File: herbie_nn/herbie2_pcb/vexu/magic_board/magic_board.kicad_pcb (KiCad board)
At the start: 2 copper layers, 70 x 50 mm, 88 parts, among them J1 4P4C, J2 Conn_ARM_JTAG_SWD_10, J3 USB_C_Receptacle_USB2.0_14P, J4 Conn_01x04_Socket, J5 Conn_01x05_Pin, J6 Conn_01x05_Pin, J7 Conn_01x05_Pin, Q2 MMBT3904, U11 74LVC125, U12 AMS1117-5.0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

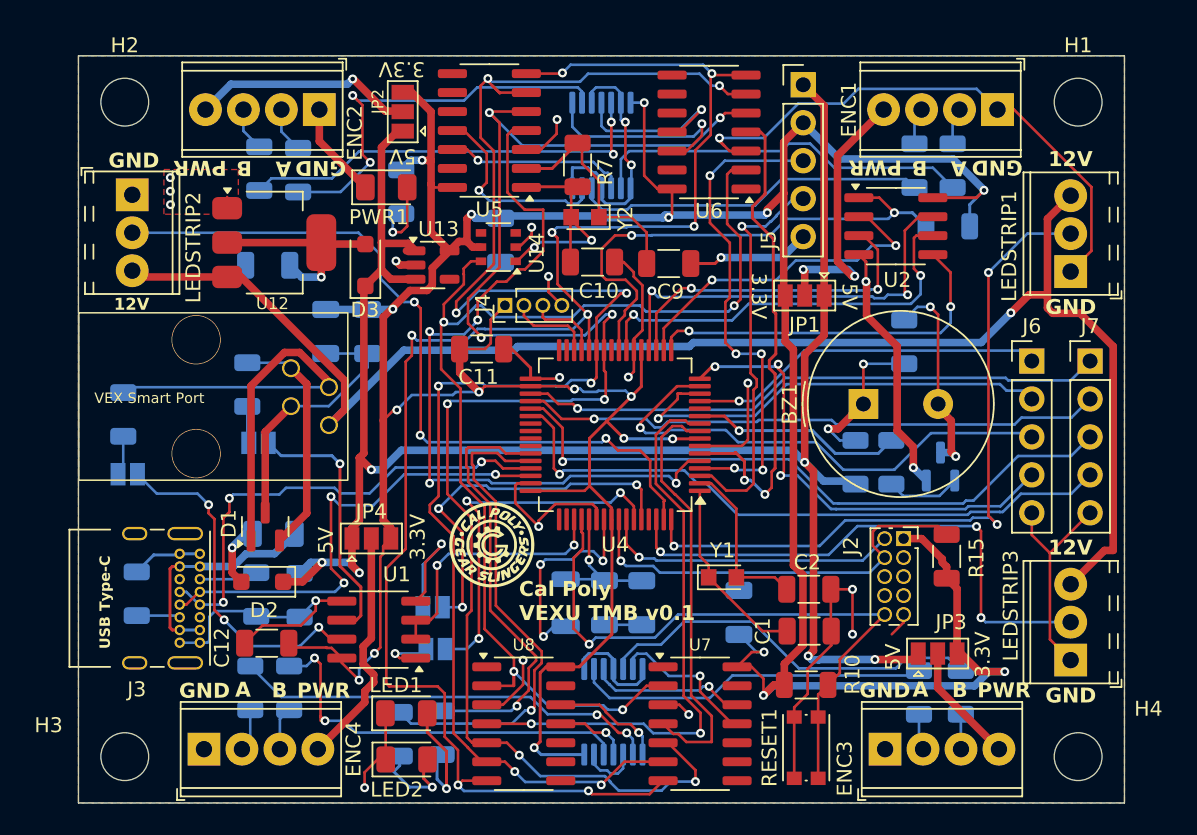
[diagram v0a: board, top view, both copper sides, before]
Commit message: added level shifters for led strips
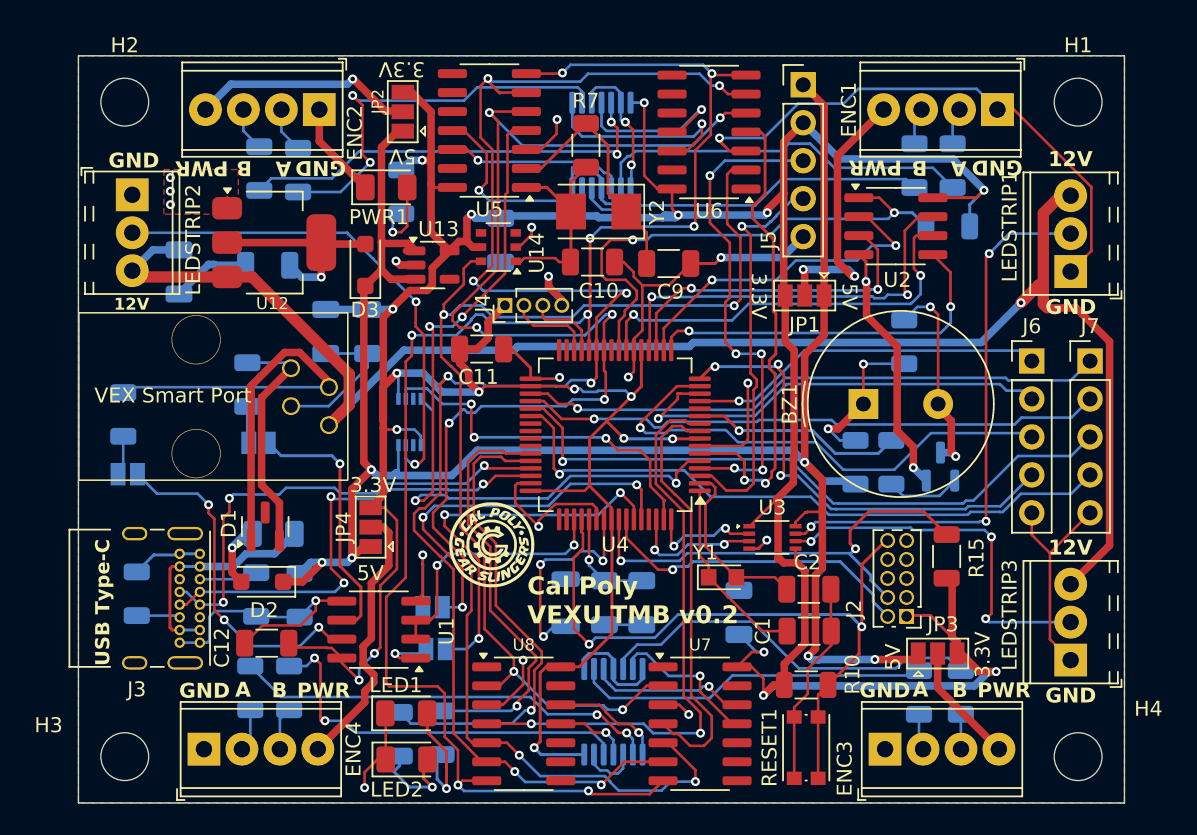
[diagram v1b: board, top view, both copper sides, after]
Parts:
- added C14: 22uF, Capacitor_SMD:C_1206_3216Metric, B.Cu at (32.2, 76.5)
- added U3: 74LVC2T45DC, Package_SO:VSSOP-8_2.3x2mm_P0.5mm, F.Cu at (71.9, 94.2)
- added U9: 74LVC2T45DC, Package_SO:VSSOP-8_2.3x2mm_P0.5mm, B.Cu at (47.7, 86.5)
- C1, C2: value 15pF -> 12pF
- R4, R5, R6: value 330 -> 2K
- Y2: footprint Crystal:Crystal_SMD_2012-2Pin_2.0x1.2mm_HandSoldering -> Crystal:Crystal_SMD_5032-2Pin_5.0x3.2mm
- moved J2 6.03 mm to (77.7, 99.5), turned to 180 degrees
- moved R7 1.42 mm to (59.5, 68.0)
- moved Y2 0.99 mm to (60.3, 72.4)
- moved JP4 0.76 mm to (45.0, 93.5), turned to 90 degrees
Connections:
- LEDSTRIP1 pad 2: /LED_SIG1 -> /LED_SIG1_OUT
- LEDSTRIP2 pad 2: /LED_SIG2 -> /LED_SIG2_OUT
- LEDSTRIP3 pad 2: /LED_SIG3 -> /LED_SIG3_OUT
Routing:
- net /LED_SIG1: track 48.3 -> 7.56 mm, vias 3 -> 2
- net /LED_SIG1_OUT: track 0.00 -> 37.2 mm, vias 0 -> 3
- net /LED_SIG2_OUT: track 0.00 -> 34.1 mm, vias 0 -> 2
- net /LED_SIG3: track 36.7 -> 8.96 mm, vias 3 -> 2
- net /LED_SIG2: track 51.5 -> 24.6 mm
- net /LED_SIG3_OUT: track 0.00 -> 25.2 mm, vias 0 -> 3
- net +3.3V: track 271.6 -> 284.4 mm, vias 19 -> 20
- net +12V: track 103.4 -> 107.9 mm
- net +5V: track 127.4 -> 131.6 mm
- net /NRESET: track 42.5 -> 46.4 mm, vias 1 -> 2
- net /MOSI: track 108.3 -> 104.8 mm
- net /SWCLK: track 28.6 -> 31.8 mm, vias 1 -> 2
- net /TX_BRAIN: track 9.30 -> 6.79 mm
- net Net-(ENC4-Pin_4): track 16.2 -> 18.4 mm
- net GND: track 233.0 -> 230.8 mm, vias 23 -> 22
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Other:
- board text added: "Cal Poly VEXU TMB v0.2"
- board text removed: "Cal Poly VEXU TMB v0.1"

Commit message: updated board
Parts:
- removed the G*** at (53.2, 94.7)
- removed JP_D+1, JP_D-1, JP_RX1, JP_TX1: Jumper, Jumper:SolderJumper-2_P1.3mm_Open_Pad1.0x1.5mm
- added F2: 1A, Fuse:Fuse_1206_3216Metric, F.Cu at (45.5, 82.1)
- added G***: LOGO, js_magic_board:logo.mod1, F.Cu at (51.8, 94.6)
- added PWR2: Jumper, Jumper:SolderJumper-2_P1.3mm_Open_Pad1.0x1.5mm, F.Cu at (45.1, 86.2)
- added TP1: TestPoint, TestPoint:TestPoint_Pad_1.0x1.0mm, F.Cu at (52.6, 85.5)
- added TP2: TestPoint, TestPoint:TestPoint_Pad_1.0x1.0mm, F.Cu at (52.6, 87.6)
- R13: value R -> 0K
- moved C11 0.48 mm to (53.0, 81.7)
- moved R14 0.47 mm to (80.8, 80.7)
- moved J4 0.25 mm to (54.3, 78.7)
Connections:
- D3 pad 1: +5V -> Net-(D3-K)
- J1 pad 4: +12V -> Net-(PWR2-A)
- J4 pad 1: +3.3V -> /SCL
- J4 pad 2: /SCL -> /SDA
- J4 pad 3: /SDA -> +3.3V
- LEDSTRIP1 pad 1: GND -> +5V
- LEDSTRIP1 pad 3: +12V -> GND
- LEDSTRIP2 pad 1: GND -> +5V
- LEDSTRIP2 pad 3: +12V -> GND
- LEDSTRIP3 pad 1: GND -> +5V
- LEDSTRIP3 pad 3: +12V -> GND
- R1 pad 1: Net-(JP_D+1-B) -> Net-(U1-A)
- R2 pad 1: Net-(JP_D-1-B) -> Net-(U1-B)
- U1 pad 6: Net-(JP_D+1-A) -> Net-(U1-A)
- U1 pad 7: Net-(JP_D-1-A) -> Net-(U1-B)
- U4 pad 39: unconnected-(U4-PB16-Pad39) -> Net-(U4-PB16)
- U4 pad 40: unconnected-(U4-PB17-Pad40) -> Net-(U4-PB17)
- U4 pad 59: Net-(JP_RX1-A) -> /RX_BRAIN
- U4 pad 60: Net-(JP_TX1-A) -> /TX_BRAIN
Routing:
- net +12V: track 107.9 -> 20.1 mm
- net +5V: track 131.6 -> 203.3 mm, vias 6 -> 11
- net /RX_BRAIN: track 3.70 -> 34.0 mm, vias 1 -> 4
- net /TX_BRAIN: track 6.79 -> 34.7 mm, vias 1 -> 4
- net Net-(JP_RX1-A): track 26.3 -> 0.00 mm, vias 3 -> 0
- net Net-(JP_TX1-A): track 26.2 -> 0.00 mm, vias 3 -> 0
- net Net-(U1-B): track 0.00 -> 25.8 mm, vias 0 -> 3
- net Net-(JP_D-1-A): track 23.2 -> 0.00 mm, vias 3 -> 0
- net Net-(U1-A): track 0.00 -> 21.3 mm, vias 0 -> 1
- net Net-(JP_D+1-A): track 17.5 -> 0.00 mm, vias 1 -> 0
- net GND: track 230.8 -> 214.1 mm
- net /D+: track 31.9 -> 40.9 mm
- net /ENC1_SS: track 51.0 -> 45.9 mm
- net /D-: track 31.9 -> 37.0 mm
- net Net-(D3-K): track 0.00 -> 3.72 mm
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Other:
- board text removed: "12V"

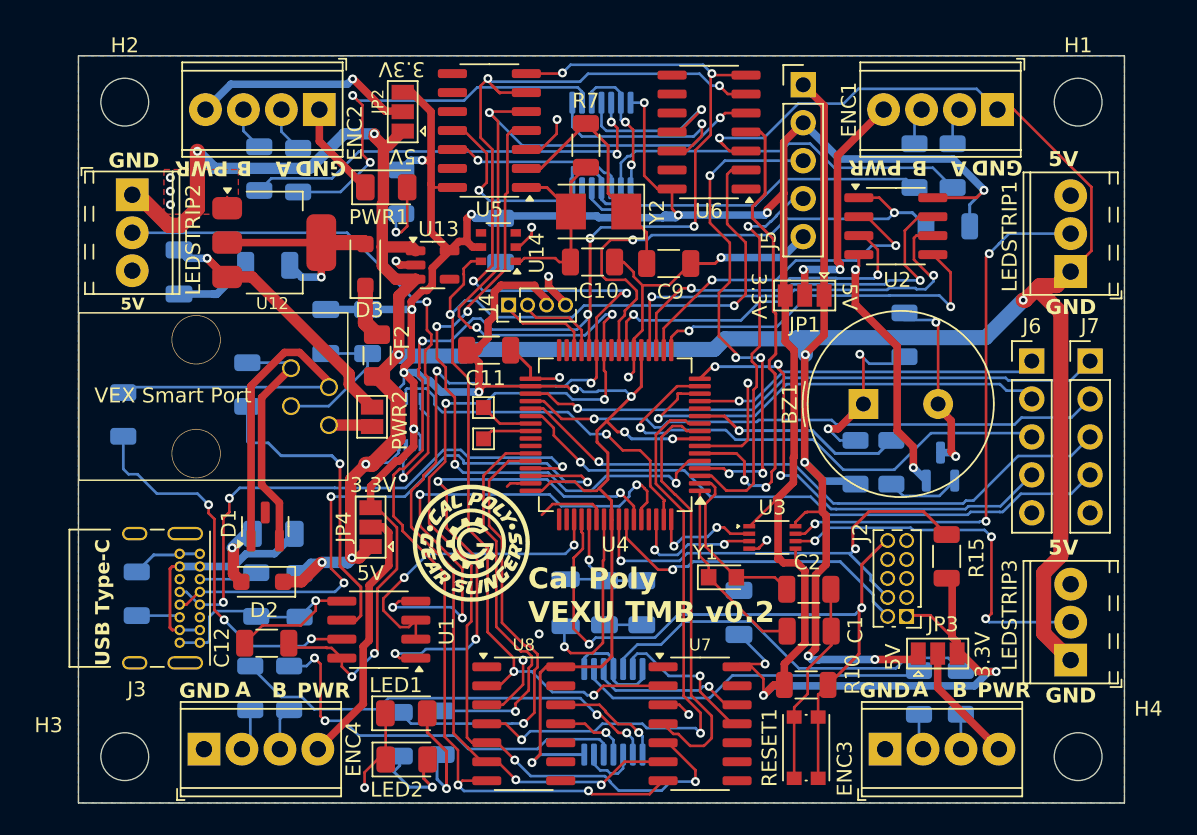
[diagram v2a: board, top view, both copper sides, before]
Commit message: removed qspi flash
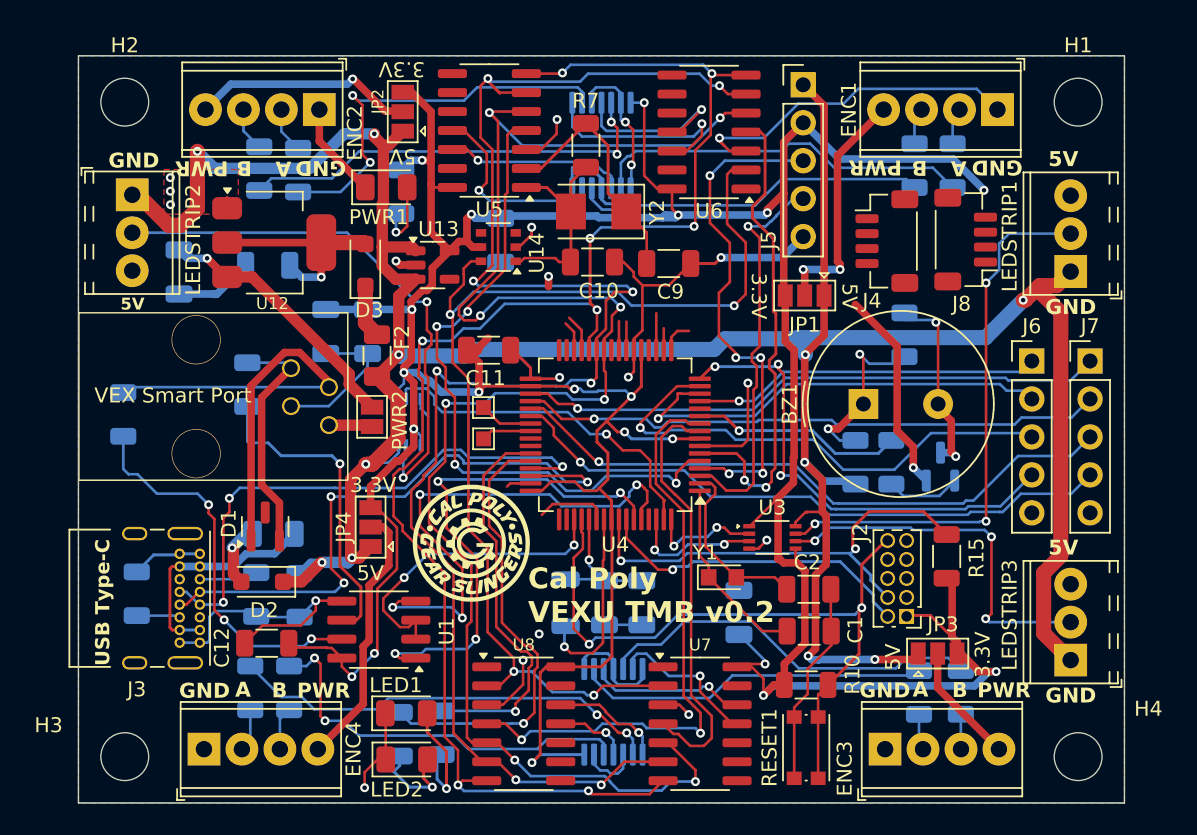
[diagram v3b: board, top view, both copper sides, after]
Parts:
- removed R8: 10K, Resistor_SMD:R_1206_3216Metric
- removed U2: AT25SF081-SSHD-X, Package_SO:SOIC-8_3.9x4.9mm_P1.27mm
- added J8: Conn_01x04_Socket, Connector_JST:JST_SH_BM04B-SRSS-TB_1x04-1MP_P1.00mm_Vertical, F.Cu at (84.9, 74.3)
- J4: footprint Connector_PinHeader_1.27mm:PinHeader_1x04_P1.27mm_Vertical -> Connector_JST:JST_SH_BM04B-SRSS-TB_1x04-1MP_P1.00mm_Vertical
- moved J4 25.7 mm to (79.6, 74.4), turned to -90 degrees
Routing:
- net /QSPI_CS: track 34.9 -> 1.94 mm, vias 2 -> 0
- net /QSPI_DATA3: track 27.9 -> 0.00 mm, vias 2 -> 0
- net /QSPI_SCK: track 28.9 -> 1.91 mm, vias 2 -> 0
- net /QSPI_DATA0: track 25.0 -> 2.23 mm, vias 2 -> 0
- net /QSPI_DATA1: track 22.6 -> 1.47 mm, vias 2 -> 0
- net GND: track 214.1 -> 194.0 mm, vias 22 -> 21
- net /QSPI_DATA2: track 21.8 -> 2.47 mm, vias 2 -> 0
- net +3.3V: track 286.5 -> 272.2 mm
- net /SCL: track 6.58 -> 2.03 mm
- net /SDA: track 5.89 -> 2.51 mm
- net /SCK: track 109.7 -> 111.0 mm
- net /MISO: track 108.4 -> 109.5 mm
- net /MOSI: track 102.6 -> 103.2 mm

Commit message: added qwiic connectors
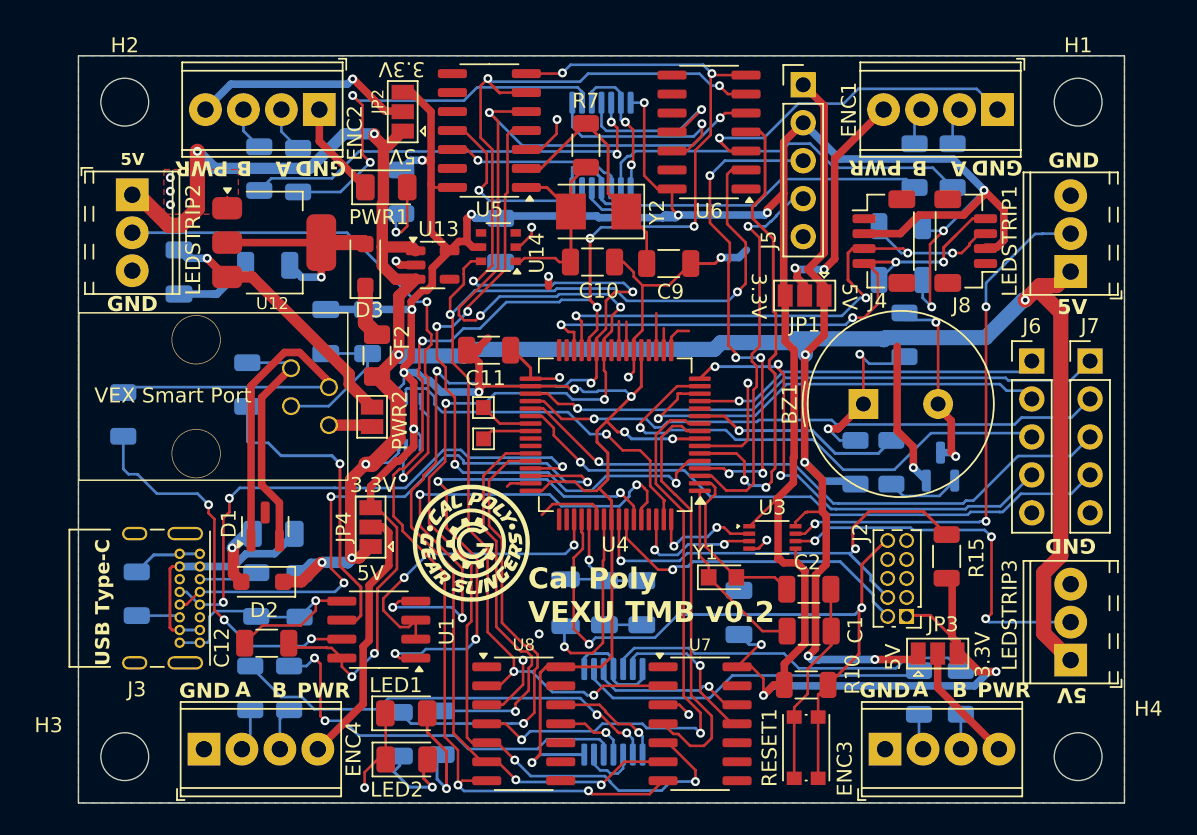
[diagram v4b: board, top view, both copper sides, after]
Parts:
- added R16: 4.7K, Resistor_SMD:R_1206_3216Metric, B.Cu at (80.5, 77.0)
- added R8: 4.7K, Resistor_SMD:R_1206_3216Metric, B.Cu at (80.5, 73.4)
- moved J4 0.20 mm to (79.4, 74.4)
- moved J8 0.10 mm to (84.9, 74.4)
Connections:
- J4 pad 1: /SCL -> GND
- J4 pad 2: /SDA -> +3.3V
- J4 pad 3: +3.3V -> /SDA
- J4 pad 4: GND -> /SCL
- J8 pad 1: /SCL -> GND
- J8 pad 2: /SDA -> +3.3V
- J8 pad 3: +3.3V -> /SDA
- J8 pad 4: GND -> /SCL
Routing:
- net /SCL: track 2.03 -> 38.5 mm, vias 0 -> 4
- net /SDA: track 2.51 -> 38.5 mm, vias 0 -> 4
- net +3.3V: track 272.2 -> 298.9 mm, vias 20 -> 22
- net GND: track 194.0 -> 185.9 mm
- net Net-(R25-Pad2): track 26.3 -> 24.8 mm
- net /LED_SIG1_OUT: track 37.1 -> 36.1 mm
- net +5V: track 203.3 -> 204.3 mm
- net /PA_03: track 34.2 -> 33.7 mm

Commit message: fixed ground disconnect
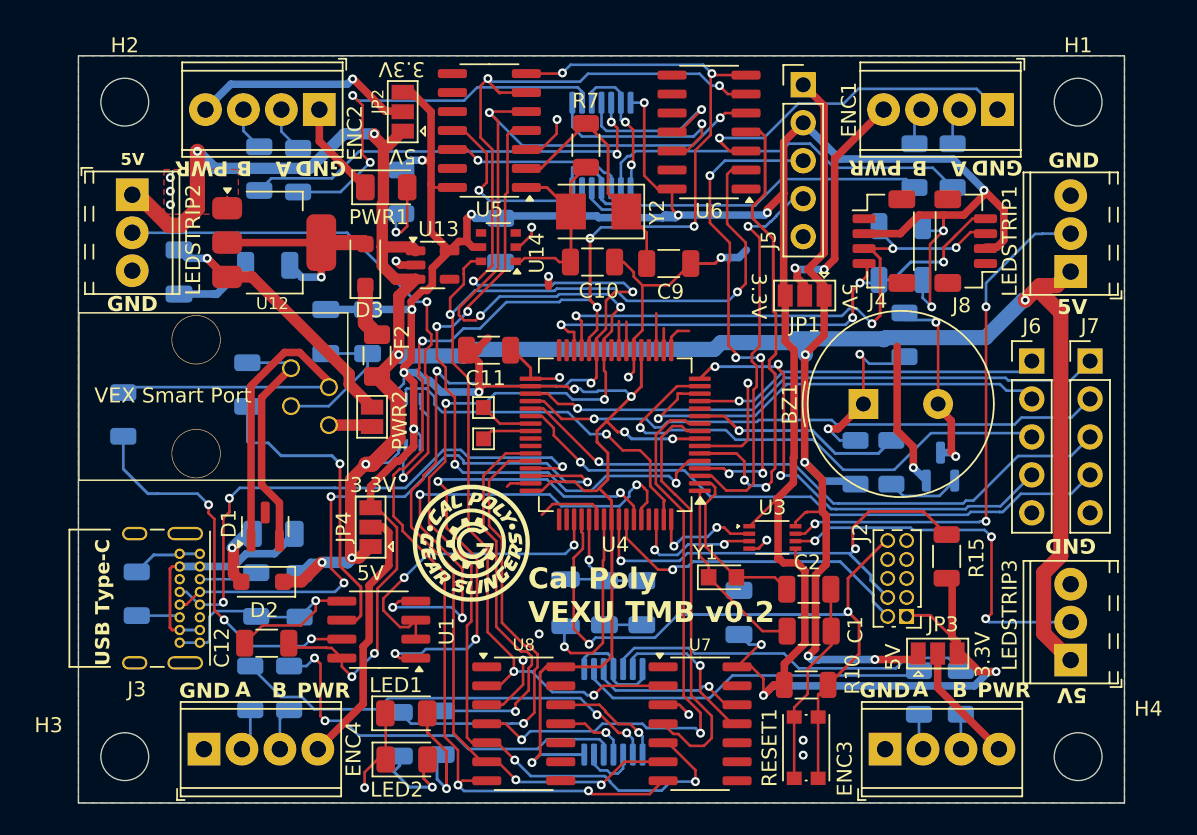
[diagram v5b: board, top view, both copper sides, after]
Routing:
- net +3.3V: track 298.9 -> 296.1 mm
- net /SCL: track 38.5 -> 36.8 mm
- net /SDA: track 38.5 -> 39.0 mm
- net GND: vias 21 -> 23
